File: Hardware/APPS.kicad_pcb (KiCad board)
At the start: 2 copper layers, 100 x 75 mm, 65 parts, among them J4 Sygnały, J5 Diagnostyka, J8 Zasilanie+CAN, K1 FINDER-30.22, Q1 BSS138, SW1 SW_Push, U1 STM32L4P5RET6, U3 LM1117-3.3, U4 LM1117-3.3, U5 LM1117-3.3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

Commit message: Generated BOM
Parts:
- R11, R13, R15, R17: footprint Resistor_SMD:R_1206_3216Metric -> Resistor_SMD:R_0603_1608Metric_Pad0.98x0.95mm_HandSolder
- moved R17 0.56 mm to (151.1, 54.2)
- moved R15 0.54 mm to (146.7, 54.2)
- moved R13 0.53 mm to (155.1, 65.4)
- moved R11 0.51 mm to (152.6, 65.4)
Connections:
- C6 pad 1: /NRST -> NRST
- J5 pad 5: RST -> NRST
- R1 pad 1: /NRST -> NRST
- SW1 pad 2: /NRST -> NRST
- U1 pad 7: /NRST -> NRST
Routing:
- net NRST: track 0.00 -> 43.5 mm
- net /NRST: track 23.7 -> 0.00 mm
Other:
- board text removed: "SAFETY-IN"
- board text removed: "SAFETY-OUT"

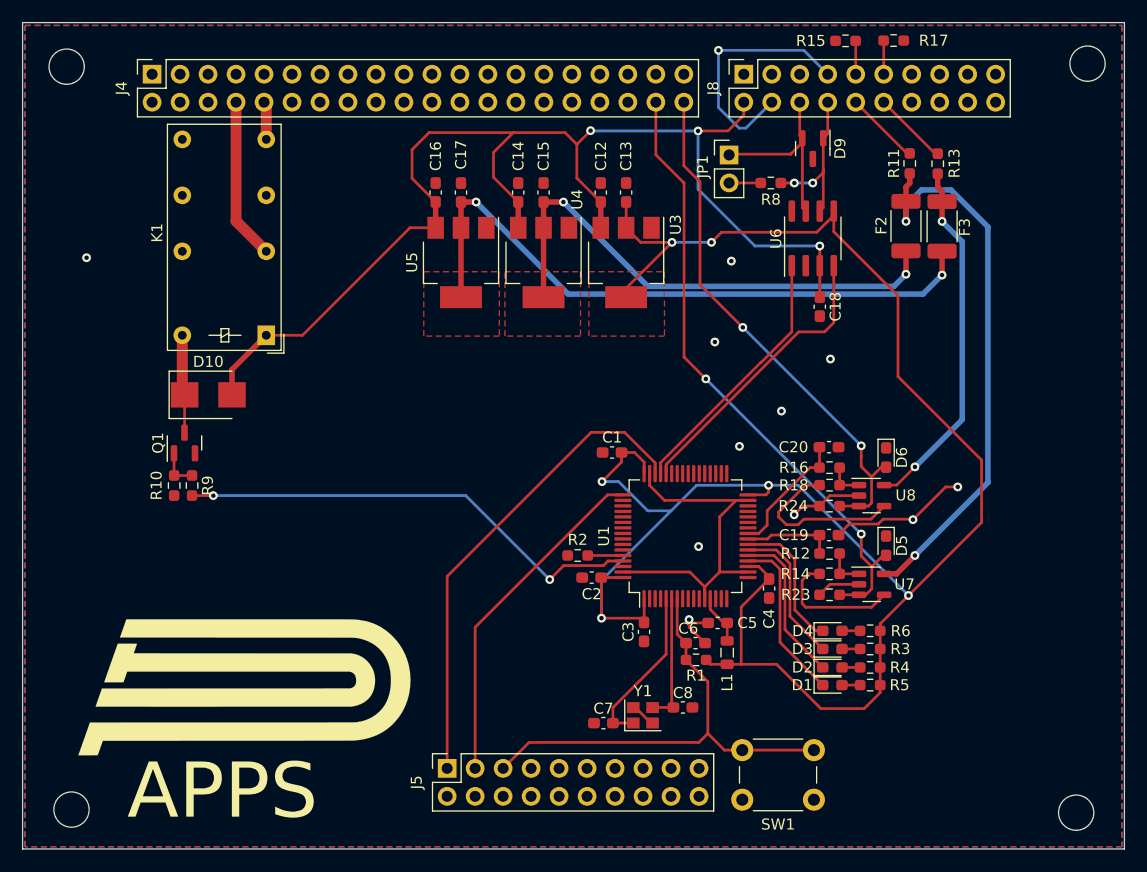
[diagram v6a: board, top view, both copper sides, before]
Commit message: Switch STM capacitors' positions, added mounting
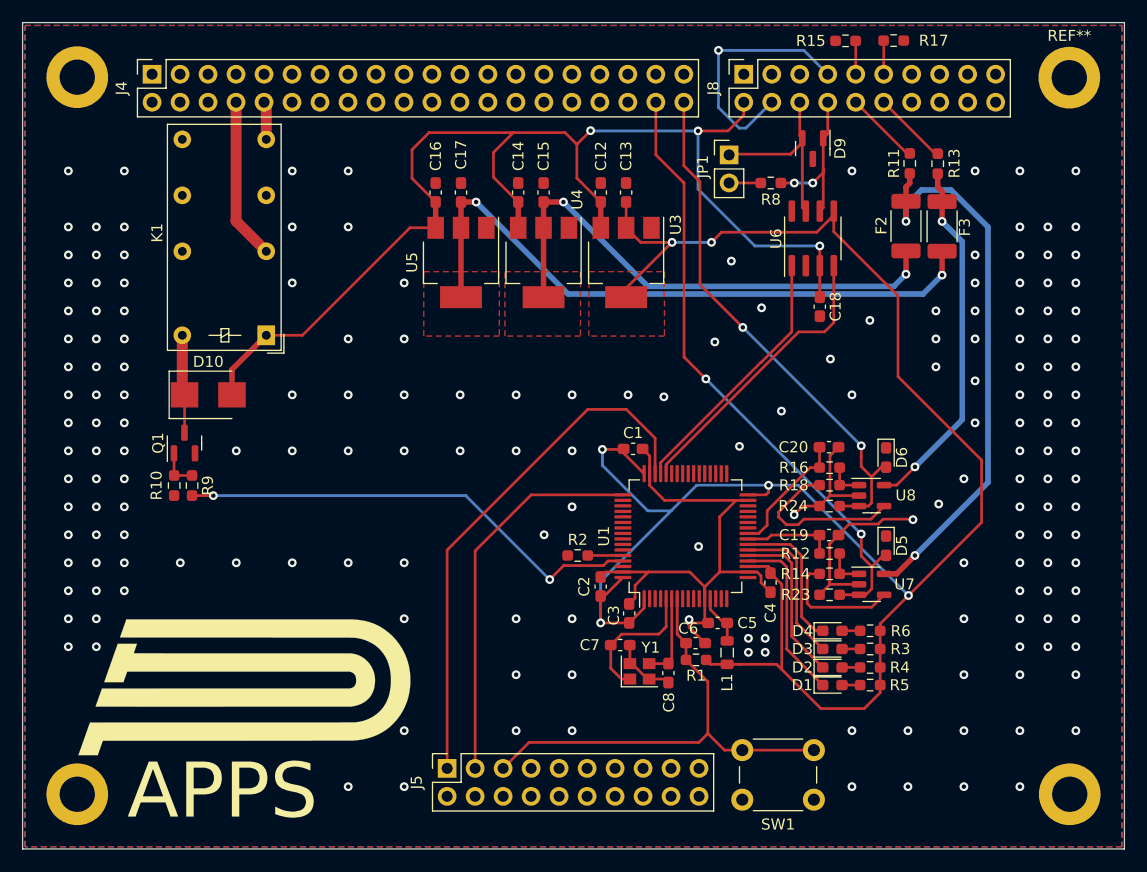
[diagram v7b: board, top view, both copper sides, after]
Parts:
- added ?: , , F.Cu at (77.0, 57.5)
- added ?: , , F.Cu at (167.1, 122.6)
- added ?: , , F.Cu at (77.0, 122.6)
- added REF**: MountingHole_3.2mm_M3_DIN965_Pad, MountingHole:MountingHole_3.2mm_M3_DIN965_Pad, F.Cu at (167.0, 57.6)
- moved C7 7.25 mm to (126.3, 109.1), turned to 0 degrees
- moved Y1 4.00 mm to (128.0, 111.5)
- moved C8 3.39 mm to (130.7, 111.6), turned to -90 degrees
- moved C3 2.15 mm to (127.1, 106.2), turned to 90 degrees
- moved C1 1.93 mm to (127.5, 91.3), turned to 0 degrees
- moved C2 1.15 mm to (124.5, 103.8), turned to 90 degrees
- moved C4 0.55 mm to (139.9, 103.4)
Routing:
- net GND: track 84.8 -> 106.3 mm, vias 12 -> 182
- net SWD: track 43.9 -> 48.3 mm
- net /XTAL2: track 11.8 -> 7.76 mm
- net CLK: track 31.2 -> 35.3 mm
- net /XTAL1: track 15.1 -> 12.5 mm
- net Net-(R14-Pad2): track 12.0 -> 11.3 mm
- net /LED3: track 13.3 -> 13.9 mm
- net /LED4: track 12.7 -> 13.3 mm
- net /LED2: track 14.4 -> 14.9 mm
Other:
- outline, holes or cut-outs redrawn
